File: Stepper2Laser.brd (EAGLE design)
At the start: 35.6 x 45.7 mm, 7 parts

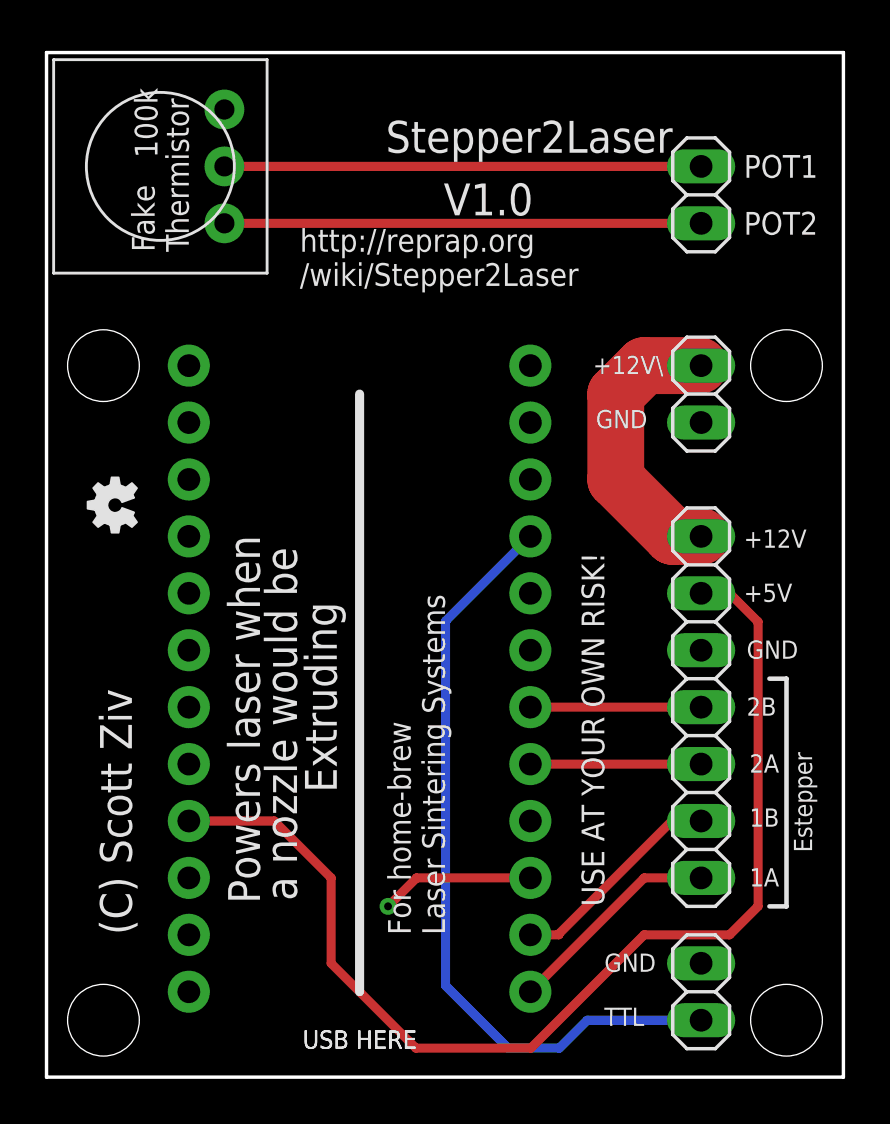
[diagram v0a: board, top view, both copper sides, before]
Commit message: Added first firmware version, fixed some trace issues.
Added firmware and minor fixes. Still in development, and relies on
retraction to work.
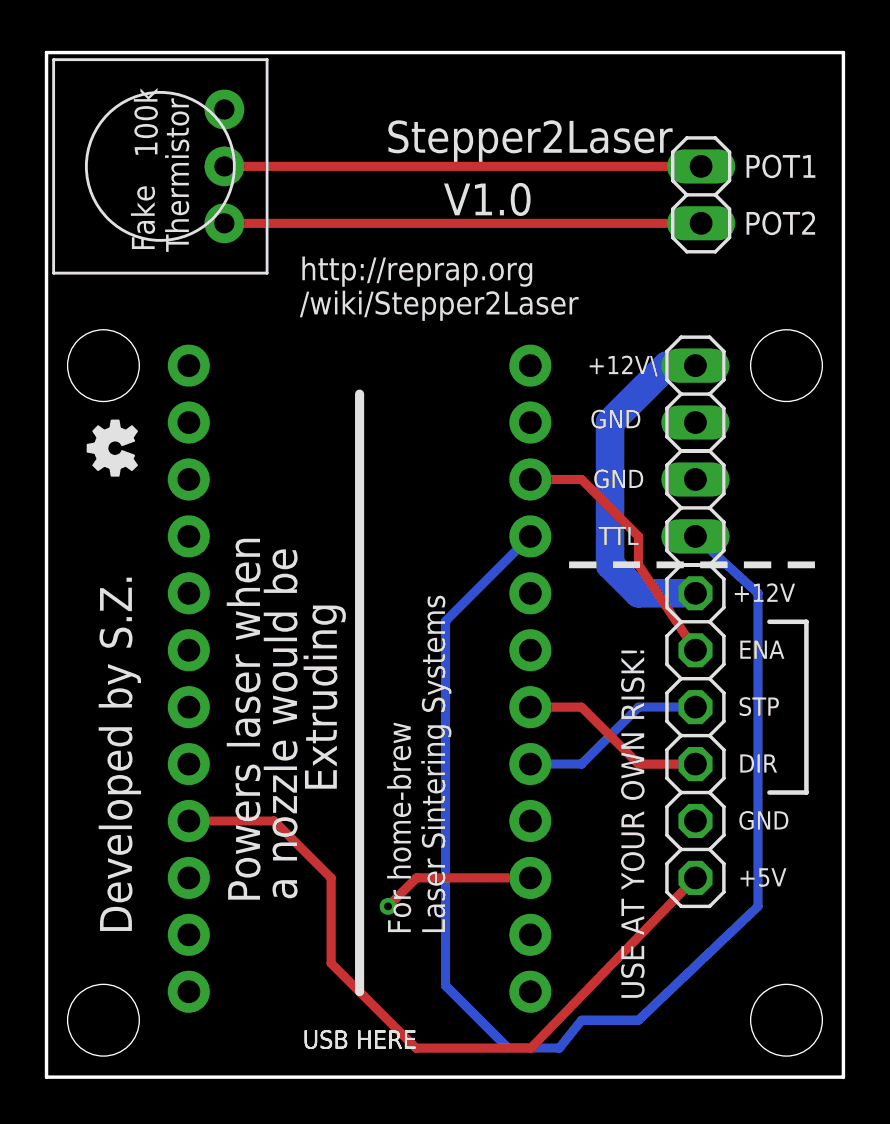
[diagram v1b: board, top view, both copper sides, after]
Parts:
- JP1: device pinhead:1X07 -> adafruit:1X06
- moved JP2 21.6 mm to (29.0, 25.4)
- moved LOGO1 2.54 mm to (3.05, 28.1)
- moved JP1 1.30 mm to (29.0, 15.2), turned to 270 degrees
- moved JP3 0.25 mm to (29.0, 30.5)
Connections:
- net 2A renamed STP
- net 2B renamed DIR
- removed net 1A: B1.1, JP1.1
- removed net 1B: B1.2, JP1.2
- new net ENA: B1.10, JP1.2
- net +12V: now also JP1.1; no longer JP1.7
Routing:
- net TTL: track 34.7 -> 57.1 mm
- net +5V: track 50.2 -> 32.3 mm
- net ENA: track 0.00 -> 11.7 mm
- net 1B: track 9.74 -> 0.00 mm
- net 1A: track 9.72 -> 0.00 mm
- net +12V: track 12.9 -> 15.5 mm
- net STP: track 7.62 -> 8.42 mm
- net DIR: track 7.62 -> 8.42 mm
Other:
- board text added: "DIR"
- board text added: "Developed by S.Z."
- board text added: "ENA"
- board text added: "STP"
- board text removed: "(C) Scott Ziv"
- board text removed: "1A"
- board text removed: "1B"
- board text removed: "2A"
- board text removed: "2B"
- board text removed: "Estepper"
